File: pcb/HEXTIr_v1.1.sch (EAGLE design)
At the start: 28 parts, among them CN1 HEX-BUS, IC1 ATMEGA328

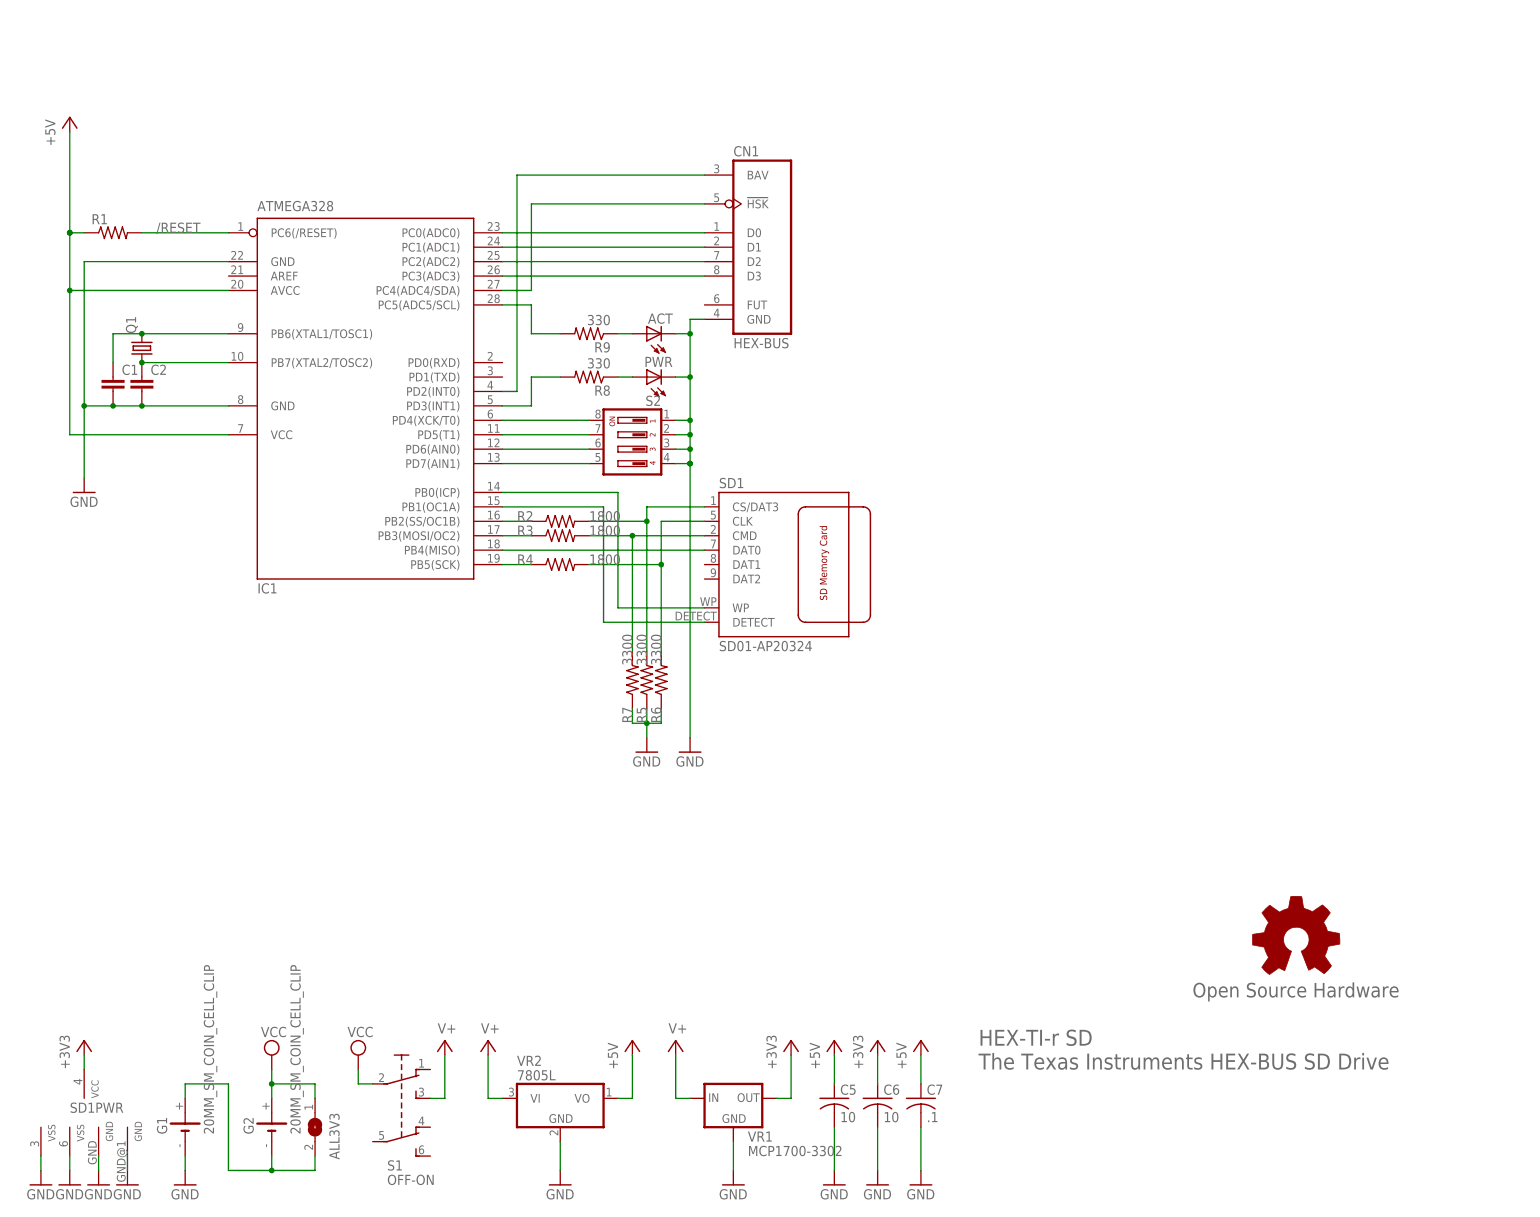
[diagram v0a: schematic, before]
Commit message: Create Arduino-compatible PCB layout
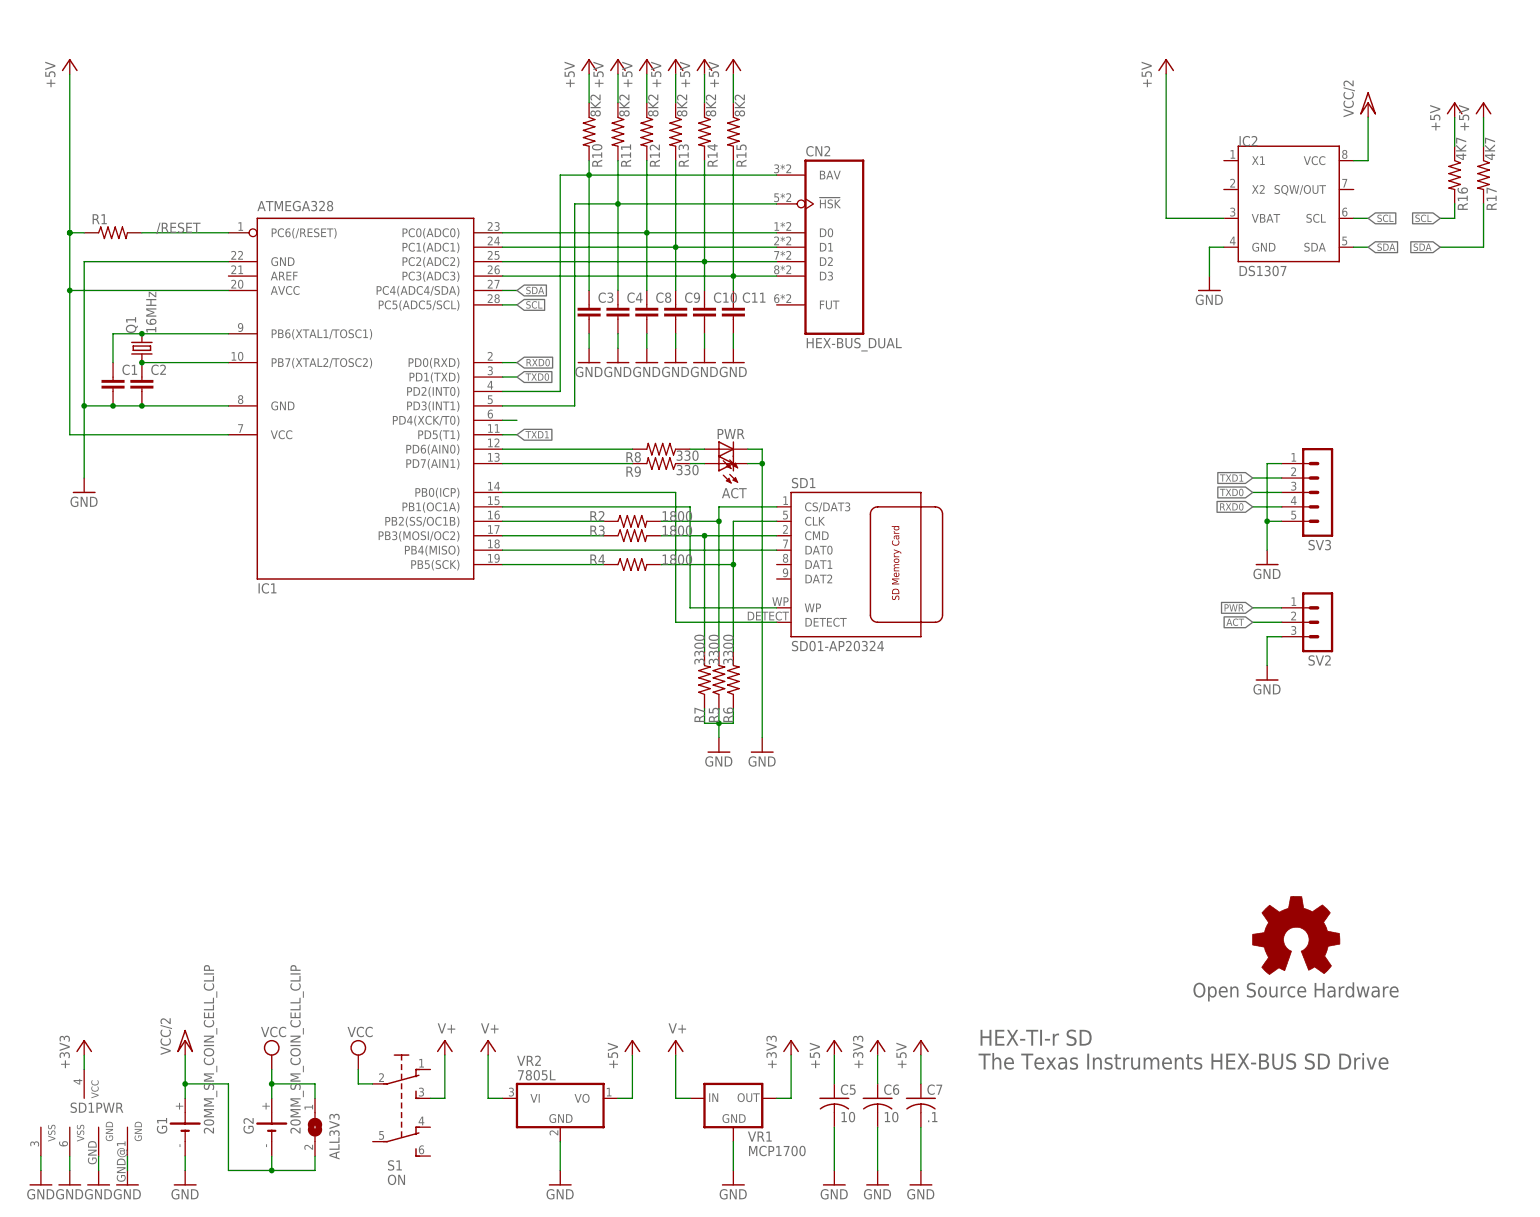
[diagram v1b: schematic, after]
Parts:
- removed CN1: HEX-BUS, ti_cc40:HEX-BUS
- removed S2: (no value), switch-dil:DP04
- added C10, C11, C3, C4, C8, C9: (no value), rcl:C-EU025-024X044
- added CN2: HEX-BUS_DUAL, ti-cc40:HEX-BUS_DUAL
- added IC2: DS1307, dallas-rtc:DS1307
- added R10, R11, R12, R13, R14, R15: 8K2, rcl:R-US_0204/2V
- added R16, R17: 4K7, rcl:R-US_0204/2V
- added SV2: (no value), con-lstb-rp:MA03-1
- added SV3: (no value), con-lstb-rp:MA05-1
- Q1: value (none) -> 16MHz
- S1: value OFF-ON -> ON
- VR1: value MCP1700-3302 -> MCP1700
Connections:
- removed net N$20: IC1.PD7(AIN1), S2.5
- removed net N$21: IC1.PD6(AIN0), S2.6
- removed net N$22: IC1.PD5(T1), S2.7
- removed net N$24: IC1.PD3(INT1), R8.2
- removed net N$25: IC1.PC5(ADC5/SCL), R9.2
- removed net N$7: ALL3V3.2, G1.+, G2.-
- new net ACT: IC1.PD7(AIN1), R9.2, SV2.2
- new net PWR: IC1.PD6(AIN0), R8.2, SV2.1
- new net RXD0: IC1.PD0(RXD), SV3.4
- new net SCL: IC1.PC5(ADC5/SCL), IC2.SCL, R16.2
- new net SDA: IC1.PC4(ADC4/SDA), IC2.SDA, R17.2
- new net TXD0: IC1.PD1(TXD), SV3.3
- new net TXD1: IC1.PD5(T1), SV3.2
- new net VCC/2: ALL3V3.2, G1.+, G2.-, IC2.VCC
- net !HSK: now also C4.1, CN2A.!HSK, IC1.PD3(INT1), R11.2; no longer CN1.!HSK, IC1.PC4(ADC4/SDA)
- net +5V: now also IC2.VBAT, R10.1, R11.1, R12.1, R13.1, R14.1, R15.1, R16.1, R17.1
- net BAV: now also C3.1, CN2A.BAV, R10.2; no longer CN1.BAV
- net D0: now also C8.1, CN2A.D0, R12.2; no longer CN1.D0
- net D1: now also C9.1, CN2A.D1, R13.2; no longer CN1.D1
- net D2: now also C10.1, CN2A.D2, R14.2; no longer CN1.D2
- net D3: now also C11.1, CN2A.D3, R15.2; no longer CN1.D3
- net GND: now also C10.2, C11.2, C3.2, C4.2, C8.2, C9.2, IC2.GND, SV2.3, SV3.1, SV3.5; no longer CN1.GND, S2.1, S2.2, S2.3, S2.4
- net N$23: no longer S2.8
- net N$5: now also IC1.PB1(OC1A); no longer IC1.PB0(ICP)
- net N$6: now also IC1.PB0(ICP); no longer IC1.PB1(OC1A)
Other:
- moved on the sheet: ACT, PWR, R2, R3, R4, R5, R6, R7, R8, R9, SD1

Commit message: Clean up old unused code fragments and start reducing dependence on str*() functions.
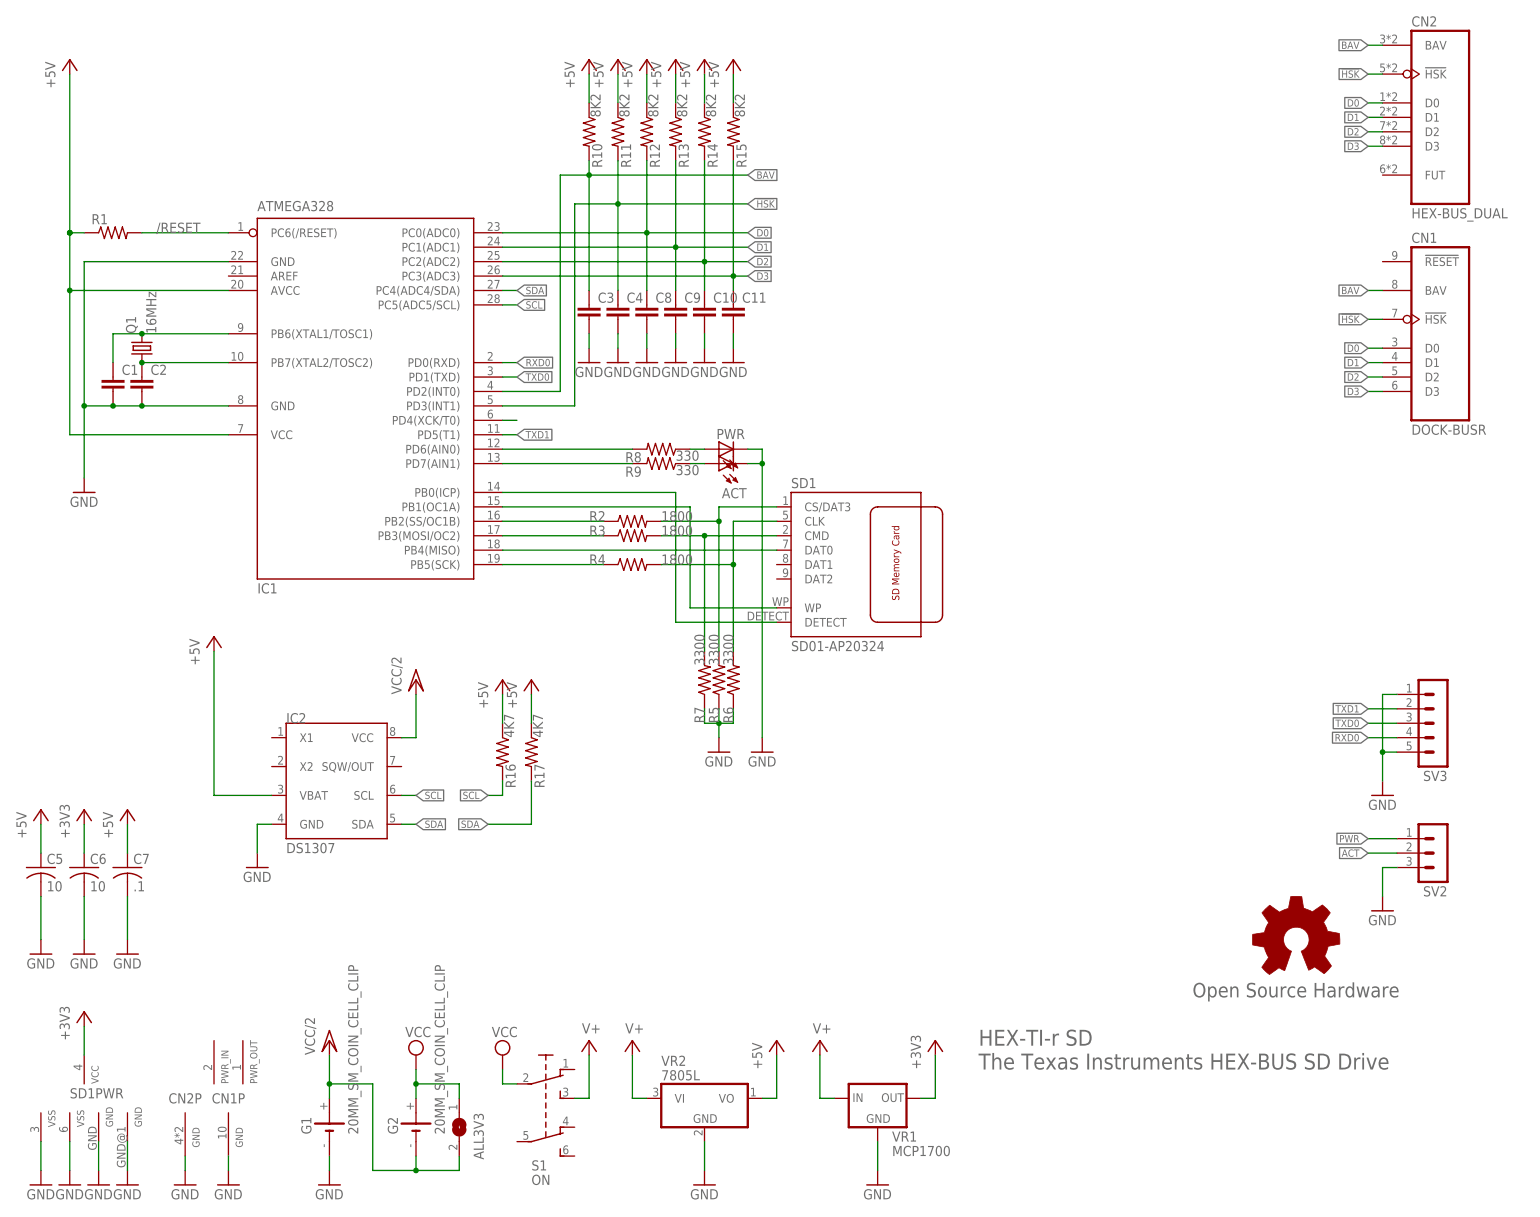
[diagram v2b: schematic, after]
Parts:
- added CN1: DOCK-BUSR, ti-cc40:DOCK-BUSR
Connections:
- net !HSK: now also CN1A.!HSK
- net BAV: now also CN1A.BAV
- net D0: now also CN1A.D0
- net D1: now also CN1A.D1
- net D2: now also CN1A.D2
- net D3: now also CN1A.D3
- net GND: now also CN1P.GND, CN2P.GND
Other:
- moved on the sheet: ALL3V3, C5, C6, C7, CN2, G1, G2, IC2, R16, R17, S1, SD1PWR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

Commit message: Modify pin settings for base config to PCB v1.1
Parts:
- R1: value (none) -> 10K
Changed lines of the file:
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@@
 <part name="GND1" library="supply1" deviceset="GND" device=""/>
 <part name="FRAME1" library="frames" deviceset="FRAME_A_L" device="" value="FRAME_A_L"/>
-<part name="R1" library="resistor" deviceset="R-US_" device="0204/2V"/>
+<part name="R1" library="resistor" deviceset="R-US_" device="0204/2V" value="10K"/>
 <part name="SD1" library="con-atom-sd" deviceset="SD01-AP20324" device=""/>
 <part name="GND3" library="supply1" deviceset="GND" device=""/>
